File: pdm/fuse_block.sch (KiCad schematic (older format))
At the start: 12 parts, among them U12 BTS443P, U13 TLP291

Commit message: small changes
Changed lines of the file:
@@
 EESchema Schematic File Version 4
+LIBS:pdm-cache
 EELAYER 30 0
 EELAYER END
 $Descr A4 11693 8268
 encoding utf-8
-Sheet 4 6
+Sheet 5 6
 Title ""
 Date ""
@@
 AR Path="/5F956034/5F95464C" Ref="U8"  Part="1"
 AR Path="/5F9560D2/5F95464C" Ref="U10"  Part="1"
-F 0 "U4" H 5750 3325 50  0000 C CNN
+F 0 "U12" H 5750 3325 50  0000 C CNN
 F 1 "BTS443P" H 5750 3234 50  0000 C CNN
 F 2 "Package_TO_SOT_SMD:TO-252-4" H 5750 3350 50  0001 C CNN
@@
 AR Path="/5F956034/5F95465A" Ref="R12"  Part="1"
 AR Path="/5F9560D2/5F95465A" Ref="R16"  Part="1"
-F 0 "R4" V 5050 3700 50  0000 C CNN
+F 0 "R20" V 5050 3700 50  0000 C CNN
 F 1 "220R" V 5150 3700 50  0000 C CNN
 F 2 "Resistor_SMD:R_0805_2012Metric_Pad1.15x1.40mm_HandSolder" V 5080 3700 50  0001 C CNN
@@
 AR Path="/5F956034/5F954666" Ref="R11"  Part="1"
 AR Path="/5F9560D2/5F954666" Ref="R15"  Part="1"
-F 0 "R3" V 5050 3500 50  0000 C CNN
+F 0 "R19" V 5050 3500 50  0000 C CNN
 F 1 "220R" V 5150 3500 50  0000 C CNN
 F 2 "Resistor_SMD:R_0805_2012Metric_Pad1.15x1.40mm_HandSolder" V 5080 3500 50  0001 C CNN
@@
 AR Path="/5F956034/5F95466C" Ref="F3"  Part="1"
 AR Path="/5F9560D2/5F95466C" Ref="F4"  Part="1"
-F 0 "F1" V 6253 3600 50  0000 C CNN
+F 0 "F5" V 6253 3600 50  0000 C CNN
 F 1 "Fuse" V 6344 3600 50  0000 C CNN
 F 2 "Fuse:Fuse_Blade_ATO_directSolder" V 6380 3600 50  0001 C CNN
@@
 AR Path="/5F956034/5F954672" Ref="R14"  Part="1"
 AR Path="/5F9560D2/5F954672" Ref="R18"  Part="1"
-F 0 "R6" H 6800 3900 50  0000 L CNN
+F 0 "R22" H 6800 3900 50  0000 L CNN
 F 1 "220R" V 6750 3800 50  0000 L CNN
 F 2 "Resistor_SMD:R_0805_2012Metric_Pad1.15x1.40mm_HandSolder" V 6680 3900 50  0001 C CNN
@@
 AR Path="/5F956034/5F954678" Ref="H3"  Part="1"
 AR Path="/5F9560D2/5F954678" Ref="H4"  Part="1"
-F 0 "H1" V 7154 3750 50  0000 L CNN
+F 0 "H5" V 7154 3750 50  0000 L CNN
 F 1 "MountingHole_Pad" V 7245 3750 50  0000 L CNN
 F 2 "MountingHole:MountingHole_4mm_Pad_Via" H 7200 3600 50  0001 C CNN
@@
 AR Path="/5F956034/5F954690" Ref="R13"  Part="1"
 AR Path="/5F9560D2/5F954690" Ref="R17"  Part="1"
-F 0 "R5" V 6300 4300 50  0000 C CNN
+F 0 "R21" V 6300 4300 50  0000 C CNN
 F 1 "2k2" V 6400 4300 50  0000 C CNN
 F 2 "Resistor_SMD:R_0805_2012Metric_Pad1.15x1.40mm_HandSolder" V 6330 4300 50  0001 C CNN
@@
 AR Path="/5F956034/5F9546A4" Ref="U9"  Part="1"
 AR Path="/5F9560D2/5F9546A4" Ref="U11"  Part="1"
-F 0 "U5" H 7050 4725 50  0000 C CNN
+F 0 "U13" H 7050 4725 50  0000 C CNN
 F 1 "TLP291" H 7050 4634 50  0000 C CNN
 F 2 "Package_SO:SOIC-4_4.55x2.6mm_P1.27mm" H 6850 4200 50  0001 L CIN
@@
 AR Path="/5F955F6E/5FA4088A" Ref="D3"  Part="1"
 AR Path="/5F955EE4/5FA4088A" Ref="D5"  Part="1"
-F 0 "D5" H 5293 2845 50  0000 C CNN
+F 0 "D4" H 5293 2845 50  0000 C CNN
 F 1 "LED" H 5293 2936 50  0000 C CNN
 F 2 "LED_SMD:LED_0805_2012Metric_Pad1.15x1.40mm_HandSolder" H 5300 3100 50  0001 C CNN
@@
 AR Path="/5F956034/5FA411D1" Ref="R24"  Part="1"
 AR Path="/5F9560D2/5FA411D1" Ref="R23"  Part="1"
-F 0 "R27" V 4900 3100 50  0000 C CNN
+F 0 "R26" V 4900 3100 50  0000 C CNN
 F 1 "220R" V 5000 3100 50  0000 C CNN
 F 2 "Resistor_SMD:R_0805_2012Metric_Pad1.15x1.40mm_HandSolder" V 4930 3100 50  0001 C CNN
@@
 AR Path="/5F955F6E/5FA505C5" Ref="D8"  Part="1"
 AR Path="/5F955EE4/5FA505C5" Ref="D10"  Part="1"
-F 0 "D10" H 7843 4445 50  0000 C CNN
+F 0 "D9" H 7843 4445 50  0000 C CNN
 F 1 "LED" H 7843 4536 50  0000 C CNN
 F 2 "LED_SMD:LED_0805_2012Metric_Pad1.15x1.40mm_HandSolder" H 7850 4700 50  0001 C CNN
@@
 AR Path="/5F956034/5FA505CB" Ref="R29"  Part="1"
 AR Path="/5F9560D2/5FA505CB" Ref="R28"  Part="1"
-F 0 "R32" V 7450 4700 50  0000 C CNN
+F 0 "R31" V 7450 4700 50  0000 C CNN
 F 1 "220R" V 7550 4700 50  0000 C CNN
 F 2 "Resistor_SMD:R_0805_2012Metric_Pad1.15x1.40mm_HandSolder" V 7480 4700 50  0001 C CNN

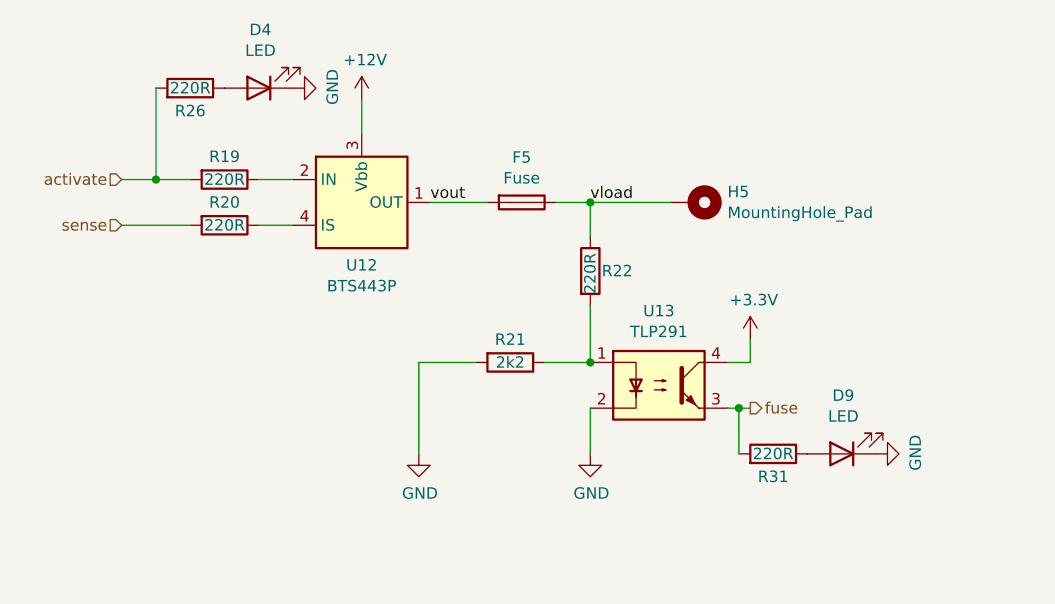
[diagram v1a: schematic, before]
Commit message: layout duplication
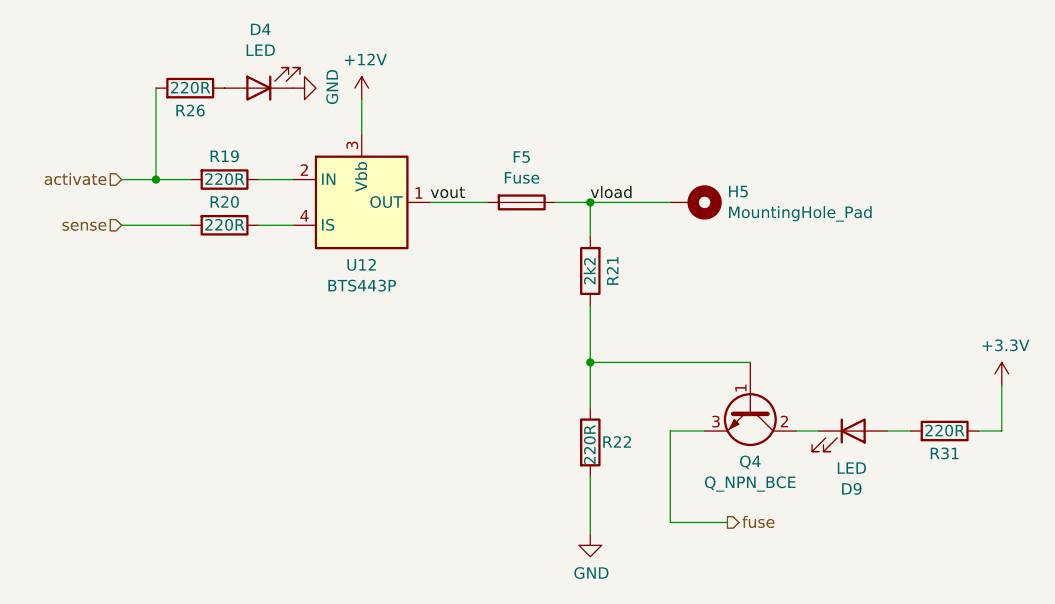
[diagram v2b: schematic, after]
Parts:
- removed U13: TLP291, Package_SO:SOIC-4_4.55x2.6mm_P1.27mm, symbol Isolator:TLP291
- added Q3: Q_NPN_BCE, Package_TO_SOT_SMD:SOT-23_Handsoldering, symbol Device:Q_NPN_BCE
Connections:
- net +3V3: now also R31.1
- net GND: now also R22.2; no longer D9.1 (K), R21.2
- net fuse: now also Q3.3 (E); no longer R31.2
- net vload: now also R21.2; no longer R22.1
- net at R21.1: now also R22.1, Q3.1 (B); no longer R22.2
- net at D9.2 (A): now also R31.2; no longer R31.1
- new net: D9.1 (K), Q3.2 (C)
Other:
- moved on the sheet: R21, R22
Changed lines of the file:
@@
-$EndComp
-$Comp
-L Device:R R?
-U 1 1 5F954672
-P 6750 3900
-AR Path="/5F954672" Ref="R?"  Part="1"
-AR Path="/5F94FFF3/5F954672" Ref="R22"  Part="1"
-AR Path="/5F955EE4/5F954672" Ref="R6"  Part="1"
-AR Path="/5F955F6E/5F954672" Ref="R10"  Part="1"
-AR Path="/5F956034/5F954672" Ref="R14"  Part="1"
-AR Path="/5F9560D2/5F954672" Ref="R18"  Part="1"
-F 0 "R22" H 6800 3900 50  0000 L CNN
-F 1 "220R" V 6750 3800 50  0000 L CNN
-F 2 "Resistor_SMD:R_0805_2012Metric_Pad1.15x1.40mm_HandSolder" V 6680 3900 50  0001 C CNN
-F 3 "~" H 6750 3900 50  0001 C CNN
-	1    6750 3900
-	1    0    0    -1
 $EndComp
 $Comp
@@
 	6750 3600 7100 3600
 $Comp
-L power:GND #PWR?
-U 1 1 5F954682
-P 6750 4700
-AR Path="/5F954682" Ref="#PWR?"  Part="1"
-AR Path="/5F94FFF3/5F954682" Ref="#PWR036"  Part="1"
-AR Path="/5F955EE4/5F954682" Ref="#PWR020"  Part="1"
-AR Path="/5F955F6E/5F954682" Ref="#PWR024"  Part="1"
-AR Path="/5F956034/5F954682" Ref="#PWR028"  Part="1"
-AR Path="/5F9560D2/5F954682" Ref="#PWR032"  Part="1"
-F 0 "#PWR020" H 6750 4450 50  0001 C CNN
-F 1 "GND" H 6755 4527 50  0000 C CNN
-F 2 "" H 6750 4700 50  0001 C CNN
-F 3 "" H 6750 4700 50  0001 C CNN
-	1    6750 4700
-	1    0    0    -1
-$EndComp
-$Comp
-L power:+3.3V #PWR?
-U 1 1 5F954688
-P 7450 4200
-AR Path="/5F954688" Ref="#PWR?"  Part="1"
-AR Path="/5F94FFF3/5F954688" Ref="#PWR037"  Part="1"
-AR Path="/5F955EE4/5F954688" Ref="#PWR021"  Part="1"
-AR Path="/5F955F6E/5F954688" Ref="#PWR025"  Part="1"
-AR Path="/5F956034/5F954688" Ref="#PWR029"  Part="1"
-AR Path="/5F9560D2/5F954688" Ref="#PWR033"  Part="1"
-F 0 "#PWR021" H 7450 4050 50  0001 C CNN
-F 1 "+3.3V" H 7465 4373 50  0000 C CNN
-F 2 "" H 7450 4200 50  0001 C CNN
-F 3 "" H 7450 4200 50  0001 C CNN
-	1    7450 4200
-	1    0    0    -1
-$EndComp
-Wire Wire Line
-	7450 4200 7450 4300
-$Comp
 L Device:R R?
 U 1 1 5F954690
-P 6400 4300
+P 6750 3900
 AR Path="/5F954690" Ref="R?"  Part="1"
 AR Path="/5F94FFF3/5F954690" Ref="R21"  Part="1"
@@
 AR Path="/5F956034/5F954690" Ref="R13"  Part="1"
 AR Path="/5F9560D2/5F954690" Ref="R17"  Part="1"
-F 0 "R21" V 6300 4300 50  0000 C CNN
-F 1 "2k2" V 6400 4300 50  0000 C CNN
-F 2 "Resistor_SMD:R_0805_2012Metric_Pad1.15x1.40mm_HandSolder" V 6330 4300 50  0001 C CNN
-F 3 "~" H 6400 4300 50  0001 C CNN
-	1    6400 4300
-	0    1    1    0
+F 0 "R21" V 6650 3900 50  0000 C CNN
+F 1 "2k2" V 6750 3900 50  0000 C CNN
+F 2 "Resistor_SMD:R_0805_2012Metric_Pad1.15x1.40mm_HandSolder" V 6680 3900 50  0001 C CNN
+F 3 "~" H 6750 3900 50  0001 C CNN
+	1    6750 3900
+	-1   0    0    1
 $EndComp
 $Comp
 L power:GND #PWR?
 U 1 1 5F954696
-P 6000 4700
+P 6750 5050
 AR Path="/5F954696" Ref="#PWR?"  Part="1"
 AR Path="/5F94FFF3/5F954696" Ref="#PWR035"  Part="1"
@@
 AR Path="/5F956034/5F954696" Ref="#PWR027"  Part="1"
 AR Path="/5F9560D2/5F954696" Ref="#PWR031"  Part="1"
-F 0 "#PWR019" H 6000 4450 50  0001 C CNN
-F 1 "GND" H 6005 4527 50  0000 C CNN
-F 2 "" H 6000 4700 50  0001 C CNN
-F 3 "" H 6000 4700 50  0001 C CNN
-	1    6000 4700
-	1    0    0    -1
-$EndComp
-Wire Wire Line
-	6000 4700 6000 4300
-Wire Wire Line
-	7450 4300 7350 4300
-Wire Wire Line
-	7350 4500 7400 4500
-Wire Wire Line
-	6750 4500 6750 4700
-Connection ~ 6750 4300
-Wire Wire Line
-	6550 4300 6750 4300
-Wire Wire Line
-	6750 4050 6750 4300
-$Comp
-L Isolator:TLP291 U?
-U 1 1 5F9546A4
-P 7050 4400
-AR Path="/5F9546A4" Ref="U?"  Part="1"
-AR Path="/5F94FFF3/5F9546A4" Ref="U13"  Part="1"
-AR Path="/5F955EE4/5F9546A4" Ref="U5"  Part="1"
-AR Path="/5F955F6E/5F9546A4" Ref="U7"  Part="1"
-AR Path="/5F956034/5F9546A4" Ref="U9"  Part="1"
-AR Path="/5F9560D2/5F9546A4" Ref="U11"  Part="1"
-F 0 "U13" H 7050 4725 50  0000 C CNN
-F 1 "TLP291" H 7050 4634 50  0000 C CNN
-F 2 "Package_SO:SOIC-4_4.55x2.6mm_P1.27mm" H 6850 4200 50  0001 L CIN
-F 3 "https://toshiba.semicon-storage.com/info/docget.jsp?did=12884&prodName=TLP291" H 7050 4400 50  0001 L CNN
-	1    7050 4400
+F 0 "#PWR019" H 6750 4800 50  0001 C CNN
+F 1 "GND" H 6755 4877 50  0000 C CNN
+F 2 "" H 6750 5050 50  0001 C CNN
+F 3 "" H 6750 5050 50  0001 C CNN
+	1    6750 5050
 	1    0    0    -1
 $EndComp
@@
 Text HLabel 4700 3700 0    50   Input ~ 0
 sense
-Text HLabel 7450 4500 2    50   Output ~ 0
-fuse
 Text Label 6050 3600 0    50   ~ 0
 vout
 Wire Wire Line
 	6050 3600 6300 3600
-Wire Wire Line
-	6000 4300 6250 4300
 Text Label 6750 3600 0    50   ~ 0
 vload
@@
 	4850 3500 5000 3500
 $Comp
+L Device:Q_NPN_BCE Q3
+U 1 1 5F982D06
+P 7450 4500
+AR Path="/5F955F6E/5F982D06" Ref="Q3"  Part="1"
+AR Path="/5F9560D2/5F982D06" Ref="Q1"  Part="1"
+AR Path="/5F956034/5F982D06" Ref="Q2"  Part="1"
+AR Path="/5F94FFF3/5F982D06" Ref="Q4"  Part="1"
+AR Path="/5F955EE4/5F982D06" Ref="Q5"  Part="1"
+F 0 "Q4" V 7685 4500 50  0000 C CNN
+F 1 "Q_NPN_BCE" V 7776 4500 50  0000 C CNN
+F 2 "Package_TO_SOT_SMD:SOT-23_Handsoldering" H 7650 4600 50  0001 C CNN
+F 3 "~" H 7450 4500 50  0001 C CNN
+	1    7450 4500
+	0    1    1    0
+$EndComp
+$Comp
+L Device:R R?
+U 1 1 5F954672
+P 6750 4650
+AR Path="/5F954672" Ref="R?"  Part="1"
+AR Path="/5F94FFF3/5F954672" Ref="R22"  Part="1"
+AR Path="/5F955EE4/5F954672" Ref="R6"  Part="1"
+AR Path="/5F955F6E/5F954672" Ref="R10"  Part="1"
+AR Path="/5F956034/5F954672" Ref="R14"  Part="1"
+AR Path="/5F9560D2/5F954672" Ref="R18"  Part="1"
+F 0 "R22" H 6800 4650 50  0000 L CNN
+F 1 "220R" V 6750 4550 50  0000 L CNN
+F 2 "Resistor_SMD:R_0805_2012Metric_Pad1.15x1.40mm_HandSolder" V 6680 4650 50  0001 C CNN
+F 3 "~" H 6750 4650 50  0001 C CNN
+	1    6750 4650
+	1    0    0    -1
+$EndComp
+Wire Wire Line
+	6750 4050 6750 4300
+Wire Wire Line
+	6750 4800 6750 5050
+Connection ~ 6750 4300
+Wire Wire Line
+	6750 4300 6750 4500
+Wire Wire Line
+	6750 4300 7450 4300
+$Comp
 L Device:LED D9
-U 1 1 5FA505C5
-P 7850 4700
-AR Path="/5F94FFF3/5FA505C5" Ref="D9"  Part="1"
-AR Path="/5F9560D2/5FA505C5" Ref="D6"  Part="1"
-AR Path="/5F956034/5FA505C5" Ref="D7"  Part="1"
-AR Path="/5F955F6E/5FA505C5" Ref="D8"  Part="1"
-AR Path="/5F955EE4/5FA505C5" Ref="D10"  Part="1"
-F 0 "D9" H 7843 4445 50  0000 C CNN
-F 1 "LED" H 7843 4536 50  0000 C CNN
-F 2 "LED_SMD:LED_0805_2012Metric_Pad1.15x1.40mm_HandSolder" H 7850 4700 50  0001 C CNN
-F 3 "~" H 7850 4700 50  0001 C CNN
-	1    7850 4700
-	-1   0    0    1
-$EndComp
-$Comp
-L Device:R R?
-U 1 1 5FA505CB
-P 7550 4700
-AR Path="/5FA505CB" Ref="R?"  Part="1"
-AR Path="/5F94FFF3/5FA505CB" Ref="R31"  Part="1"
-AR Path="/5F955EE4/5FA505CB" Ref="R32"  Part="1"
-AR Path="/5F955F6E/5FA505CB" Ref="R30"  Part="1"
-AR Path="/5F956034/5FA505CB" Ref="R29"  Part="1"
-AR Path="/5F9560D2/5FA505CB" Ref="R28"  Part="1"
-F 0 "R31" V 7450 4700 50  0000 C CNN
-F 1 "220R" V 7550 4700 50  0000 C CNN
-F 2 "Resistor_SMD:R_0805_2012Metric_Pad1.15x1.40mm_HandSolder" V 7480 4700 50  0001 C CNN
-F 3 "~" H 7550 4700 50  0001 C CNN
-	1    7550 4700
+U 1 1 5F98650F
+P 7900 4600
+AR Path="/5F94FFF3/5F98650F" Ref="D9"  Part="1"
+AR Path="/5F9560D2/5F98650F" Ref="D6"  Part="1"
+AR Path="/5F956034/5F98650F" Ref="D7"  Part="1"
+AR Path="/5F955F6E/5F98650F" Ref="D8"  Part="1"
+AR Path="/5F955EE4/5F98650F" Ref="D10"  Part="1"
+F 0 "D9" H 7893 4345 50  0000 C CNN
+F 1 "LED" H 7893 4436 50  0000 C CNN
+F 2 "LED_SMD:LED_0805_2012Metric_Pad1.15x1.40mm_HandSolder" H 7900 4600 50  0001 C CNN
+F 3 "~" H 7900 4600 50  0001 C CNN
+	1    7900 4600
+	1    0    0    -1
+$EndComp
+Wire Wire Line
+	7750 4600 7650 4600
+$Comp
+L Device:R R?
+U 1 1 5F986EB2
+P 8300 4600
+AR Path="/5F986EB2" Ref="R?"  Part="1"
+AR Path="/5F94FFF3/5F986EB2" Ref="R31"  Part="1"
+AR Path="/5F955EE4/5F986EB2" Ref="R32"  Part="1"
+AR Path="/5F955F6E/5F986EB2" Ref="R30"  Part="1"
+AR Path="/5F956034/5F986EB2" Ref="R29"  Part="1"
+AR Path="/5F9560D2/5F986EB2" Ref="R28"  Part="1"
+F 0 "R31" V 8200 4600 50  0000 C CNN
+F 1 "220R" V 8300 4600 50  0000 C CNN
+F 2 "Resistor_SMD:R_0805_2012Metric_Pad1.15x1.40mm_HandSolder" V 8230 4600 50  0001 C CNN
+F 3 "~" H 8300 4600 50  0001 C CNN
+	1    8300 4600
 	0    1    -1   0
 $EndComp
-$Comp
-L power:GND #PWR?
-U 1 1 5FA505D1
-P 8000 4700
-AR Path="/5FA505D1" Ref="#PWR?"  Part="1"
-AR Path="/5F94FFF3/5FA505D1" Ref="#PWR057"  Part="1"
-AR Path="/5F955EE4/5FA505D1" Ref="#PWR058"  Part="1"
-AR Path="/5F955F6E/5FA505D1" Ref="#PWR056"  Part="1"
-AR Path="/5F956034/5FA505D1" Ref="#PWR015"  Part="1"
-AR Path="/5F9560D2/5FA505D1" Ref="#PWR07"  Part="1"
-F 0 "#PWR058" H 8000 4450 50  0001 C CNN
-F 1 "GND" H 8005 4527 50  0000 C CNN
-F 2 "" H 8000 4700 50  0001 C CNN
-F 3 "" H 8000 4700 50  0001 C CNN
-	1    8000 4700
-	0    -1   -1   0
-$EndComp
-Wire Wire Line
-	7400 4700 7400 4500
-Connection ~ 7400 4500
-Wire Wire Line
-	7400 4500 7450 4500
+Wire Wire Line
+	8150 4600 8050 4600
+$Comp
+L power:+3.3V #PWR?
+U 1 1 5F98797F
+P 8550 4400
+AR Path="/5F98797F" Ref="#PWR?"  Part="1"
+AR Path="/5F94FFF3/5F98797F" Ref="#PWR029"  Part="1"
+AR Path="/5F955EE4/5F98797F" Ref="#PWR033"  Part="1"
+AR Path="/5F955F6E/5F98797F" Ref="#PWR025"  Part="1"
+AR Path="/5F956034/5F98797F" Ref="#PWR021"  Part="1"
+AR Path="/5F9560D2/5F98797F" Ref="#PWR015"  Part="1"
+F 0 "#PWR033" H 8550 4250 50  0001 C CNN
+F 1 "+3.3V" H 8565 4573 50  0000 C CNN
+F 2 "" H 8550 4400 50  0001 C CNN
+F 3 "" H 8550 4400 50  0001 C CNN
+	1    8550 4400
+	1    0    0    -1
+$EndComp
+Wire Wire Line
+	8550 4400 8550 4600
+Wire Wire Line
+	8550 4600 8450 4600
+Text HLabel 7350 5000 2    50   Output ~ 0
+fuse
+Wire Wire Line
+	7350 5000 7100 5000
+Wire Wire Line
+	7100 5000 7100 4600
+Wire Wire Line
+	7100 4600 7250 4600
 $EndSCHEMATC

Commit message: replaced with stm32f042
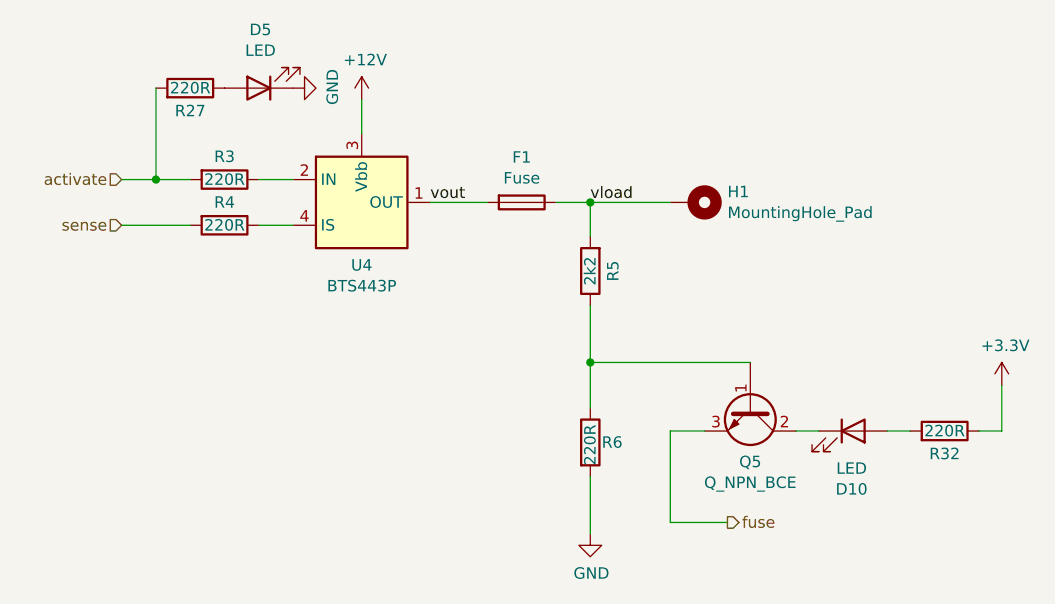
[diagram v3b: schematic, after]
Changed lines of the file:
@@
 EESchema Schematic File Version 4
-LIBS:pdm-cache
 EELAYER 30 0
 EELAYER END
@@
 AR Path="/5F956034/5F95464C" Ref="U8"  Part="1"
 AR Path="/5F9560D2/5F95464C" Ref="U10"  Part="1"
-F 0 "U12" H 5750 3325 50  0000 C CNN
+F 0 "U4" H 5750 3325 50  0000 C CNN
 F 1 "BTS443P" H 5750 3234 50  0000 C CNN
 F 2 "Package_TO_SOT_SMD:TO-252-4" H 5750 3350 50  0001 C CNN
@@
 AR Path="/5F956034/5F95465A" Ref="R12"  Part="1"
 AR Path="/5F9560D2/5F95465A" Ref="R16"  Part="1"
-F 0 "R20" V 5050 3700 50  0000 C CNN
+F 0 "R4" V 5050 3700 50  0000 C CNN
 F 1 "220R" V 5150 3700 50  0000 C CNN
 F 2 "Resistor_SMD:R_0805_2012Metric_Pad1.15x1.40mm_HandSolder" V 5080 3700 50  0001 C CNN
@@
 AR Path="/5F956034/5F954666" Ref="R11"  Part="1"
 AR Path="/5F9560D2/5F954666" Ref="R15"  Part="1"
-F 0 "R19" V 5050 3500 50  0000 C CNN
+F 0 "R3" V 5050 3500 50  0000 C CNN
 F 1 "220R" V 5150 3500 50  0000 C CNN
 F 2 "Resistor_SMD:R_0805_2012Metric_Pad1.15x1.40mm_HandSolder" V 5080 3500 50  0001 C CNN
@@
 AR Path="/5F956034/5F95466C" Ref="F3"  Part="1"
 AR Path="/5F9560D2/5F95466C" Ref="F4"  Part="1"
-F 0 "F5" V 6253 3600 50  0000 C CNN
+F 0 "F1" V 6253 3600 50  0000 C CNN
 F 1 "Fuse" V 6344 3600 50  0000 C CNN
 F 2 "Fuse:Fuse_Blade_ATO_directSolder" V 6380 3600 50  0001 C CNN
@@
 AR Path="/5F956034/5F954678" Ref="H3"  Part="1"
 AR Path="/5F9560D2/5F954678" Ref="H4"  Part="1"
-F 0 "H5" V 7154 3750 50  0000 L CNN
+F 0 "H1" V 7154 3750 50  0000 L CNN
 F 1 "MountingHole_Pad" V 7245 3750 50  0000 L CNN
 F 2 "MountingHole:MountingHole_4mm_Pad_Via" H 7200 3600 50  0001 C CNN
@@
 AR Path="/5F956034/5F954690" Ref="R13"  Part="1"
 AR Path="/5F9560D2/5F954690" Ref="R17"  Part="1"
-F 0 "R21" V 6650 3900 50  0000 C CNN
+F 0 "R5" V 6650 3900 50  0000 C CNN
 F 1 "2k2" V 6750 3900 50  0000 C CNN
 F 2 "Resistor_SMD:R_0805_2012Metric_Pad1.15x1.40mm_HandSolder" V 6680 3900 50  0001 C CNN
@@
 AR Path="/5F955F6E/5FA4088A" Ref="D3"  Part="1"
 AR Path="/5F955EE4/5FA4088A" Ref="D5"  Part="1"
-F 0 "D4" H 5293 2845 50  0000 C CNN
+F 0 "D5" H 5293 2845 50  0000 C CNN
 F 1 "LED" H 5293 2936 50  0000 C CNN
 F 2 "LED_SMD:LED_0805_2012Metric_Pad1.15x1.40mm_HandSolder" H 5300 3100 50  0001 C CNN
@@
 AR Path="/5F956034/5FA411D1" Ref="R24"  Part="1"
 AR Path="/5F9560D2/5FA411D1" Ref="R23"  Part="1"
-F 0 "R26" V 4900 3100 50  0000 C CNN
+F 0 "R27" V 4900 3100 50  0000 C CNN
 F 1 "220R" V 5000 3100 50  0000 C CNN
 F 2 "Resistor_SMD:R_0805_2012Metric_Pad1.15x1.40mm_HandSolder" V 4930 3100 50  0001 C CNN
@@
 AR Path="/5F94FFF3/5F982D06" Ref="Q4"  Part="1"
 AR Path="/5F955EE4/5F982D06" Ref="Q5"  Part="1"
-F 0 "Q4" V 7685 4500 50  0000 C CNN
+F 0 "Q5" V 7685 4500 50  0000 C CNN
 F 1 "Q_NPN_BCE" V 7776 4500 50  0000 C CNN
 F 2 "Package_TO_SOT_SMD:SOT-23_Handsoldering" H 7650 4600 50  0001 C CNN
@@
 AR Path="/5F956034/5F954672" Ref="R14"  Part="1"
 AR Path="/5F9560D2/5F954672" Ref="R18"  Part="1"
-F 0 "R22" H 6800 4650 50  0000 L CNN
+F 0 "R6" H 6800 4650 50  0000 L CNN
 F 1 "220R" V 6750 4550 50  0000 L CNN
 F 2 "Resistor_SMD:R_0805_2012Metric_Pad1.15x1.40mm_HandSolder" V 6680 4650 50  0001 C CNN
@@
 AR Path="/5F955F6E/5F98650F" Ref="D8"  Part="1"
 AR Path="/5F955EE4/5F98650F" Ref="D10"  Part="1"
-F 0 "D9" H 7893 4345 50  0000 C CNN
+F 0 "D10" H 7893 4345 50  0000 C CNN
 F 1 "LED" H 7893 4436 50  0000 C CNN
 F 2 "LED_SMD:LED_0805_2012Metric_Pad1.15x1.40mm_HandSolder" H 7900 4600 50  0001 C CNN
@@
 AR Path="/5F956034/5F986EB2" Ref="R29"  Part="1"
 AR Path="/5F9560D2/5F986EB2" Ref="R28"  Part="1"
-F 0 "R31" V 8200 4600 50  0000 C CNN
+F 0 "R32" V 8200 4600 50  0000 C CNN
 F 1 "220R" V 8300 4600 50  0000 C CNN
 F 2 "Resistor_SMD:R_0805_2012Metric_Pad1.15x1.40mm_HandSolder" V 8230 4600 50  0001 C CNN
